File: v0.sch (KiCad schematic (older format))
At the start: 20 parts, among them J1 Connector_RJ10, J10 Connector_Generic_Conn_01x02, J2 Connector_RJ10, J3 Connector_RJ10, J4 Connector_RJ10, J5 Connector_RJ10, J6 Connector_RJ10, J7 Connector_RJ10, J8 Connector_RJ10, J9 Connector_Generic_Conn_01x08, Q1 BC337, Q2 Triac_Thyristor_Mac97a8, U1 ESP32-WROOM, U2 Interface_Expansion_PCF8574, U3 Interface_Expansion_TCA9548AP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, U4 MOC3041M

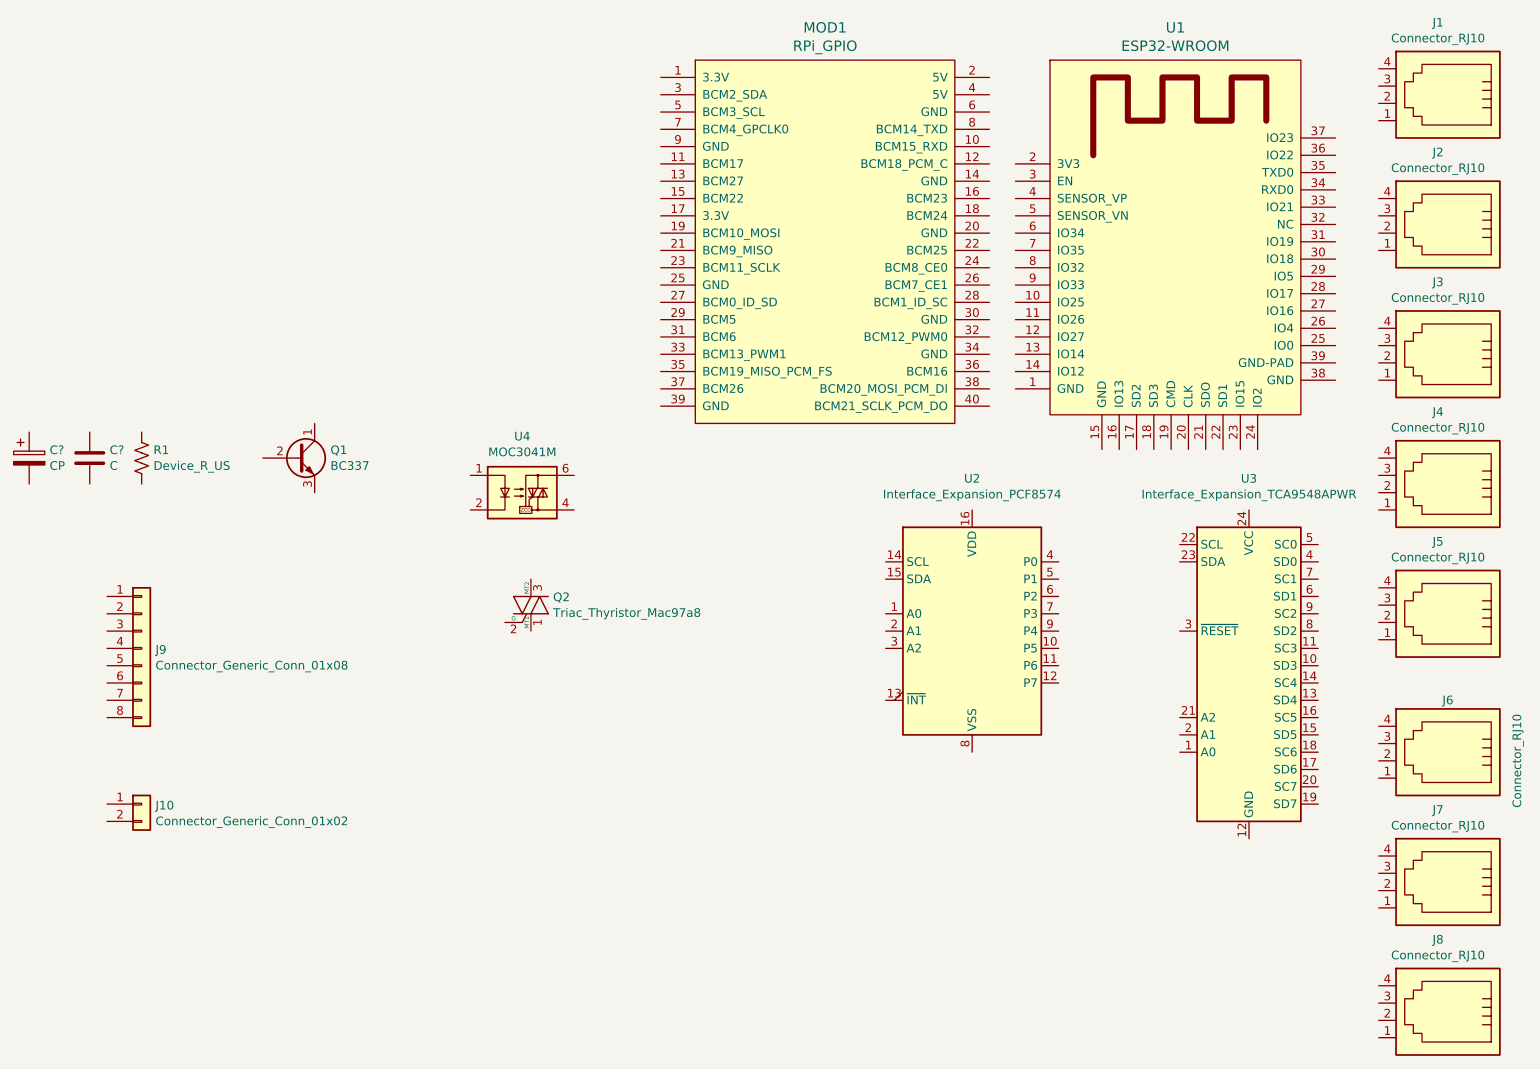
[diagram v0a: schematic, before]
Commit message: create fuente
Se creo el archivo fuente, se pusieron los componentes y se conectaron.
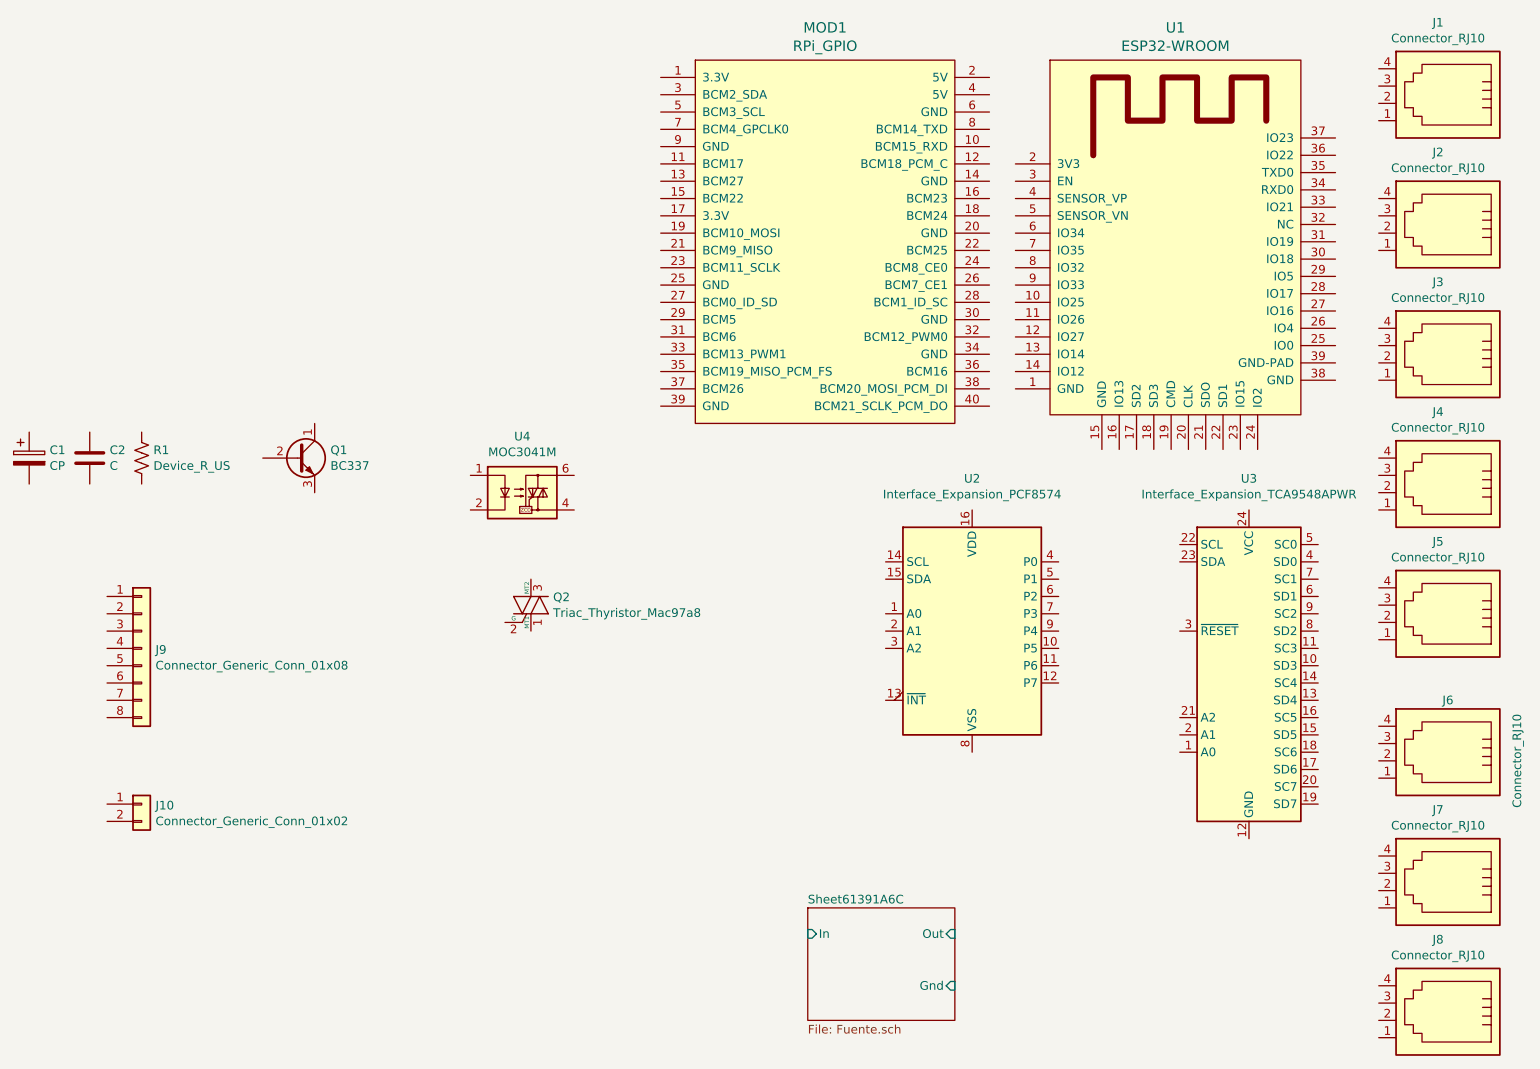
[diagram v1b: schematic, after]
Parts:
- gave numbers to parts that had none: 2
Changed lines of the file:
@@
 $Descr A4 11693 8268
 encoding utf-8
-Sheet 1 1
+Sheet 1 2
 Title ""
 Date ""
@@
 $EndComp
 $Comp
-L Device:C C?
+L Device:C C2
 U 1 1 6122D0A6
 P 2800 3100
-F 0 "C?" H 2915 3146 50  0000 L CNN
+F 0 "C2" H 2915 3146 50  0000 L CNN
 F 1 "C" H 2915 3055 50  0000 L CNN
 F 2 "" H 2838 2950 50  0001 C CNN
@@
 $EndComp
 $Comp
-L Device:CP C?
+L Device:CP C1
 U 1 1 6122DC39
 P 2450 3100
-F 0 "C?" H 2568 3146 50  0000 L CNN
+F 0 "C1" H 2568 3146 50  0000 L CNN
 F 1 "CP" H 2568 3055 50  0000 L CNN
 F 2 "" H 2488 2950 50  0001 C CNN
@@
 	1    0    0    -1
 $EndComp
+$Sheet
+S 6950 5700 850  650
+U 61391A6D
+F0 "Sheet61391A6C" 50
+F1 "Fuente.sch" 50
+F2 "In" I L 6950 5850 50
+F3 "Out" I R 7800 5850 50
+F4 "Gnd" I R 7800 6150 50
+$EndSheet
 $EndSCHEMATC
